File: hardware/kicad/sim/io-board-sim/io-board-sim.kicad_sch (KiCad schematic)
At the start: 74 parts, among them J1 to L IN combo jack, J2 to R IN combo jack, J3 to L OUT combo jack, J4 to R OUT combo jack, P1 JIO-PWR B3P-VH-B, P2 P2, P3 P3, P4 P4, P5 P5, P6 P6, U1 OPA1644AIDR, U2 OPA1656IDR, U3 OPA1656IDR, U4 OPA1656IDR

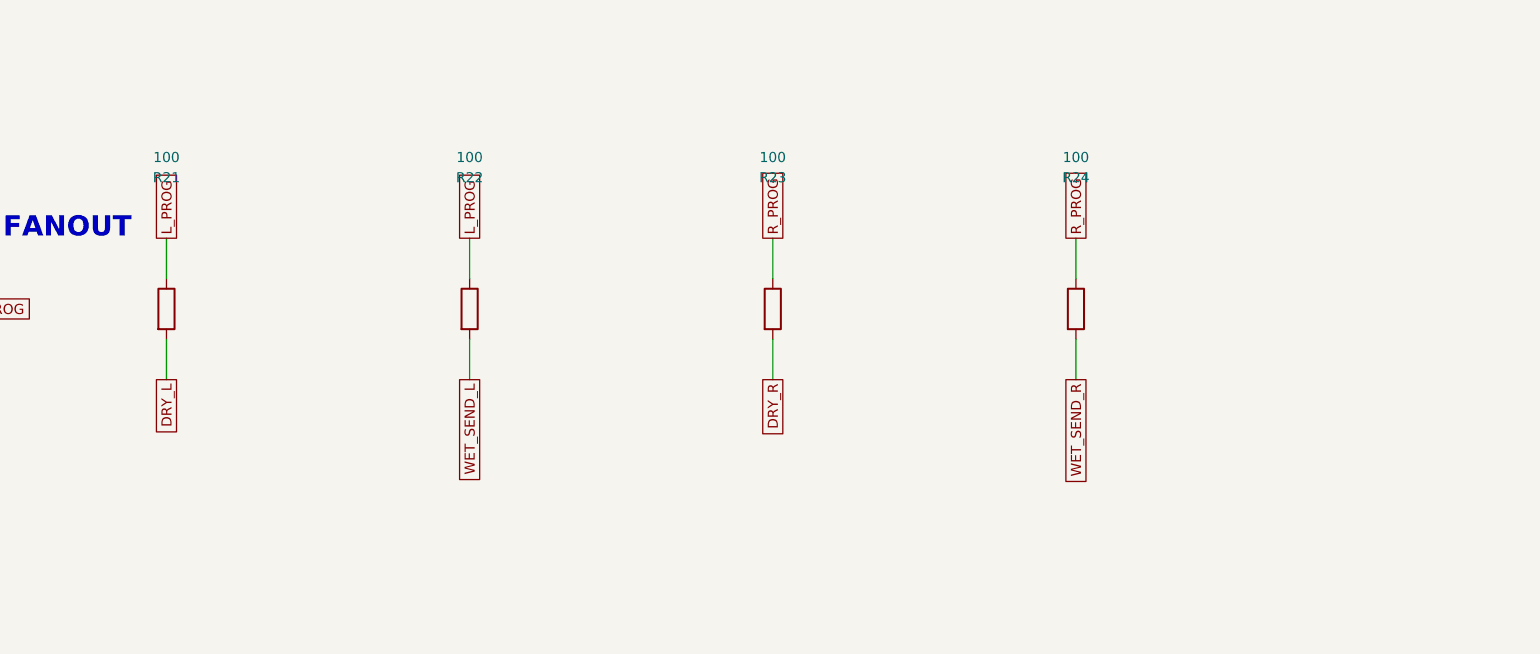
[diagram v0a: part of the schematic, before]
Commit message: Schematic review (kicad-schematic-review skill): F1 R-78E moved to +15VRAW, F2 mono-float bleed R25; both boards re-routed/verified; datasheet cache, per-instance reviews, schematic_review.md
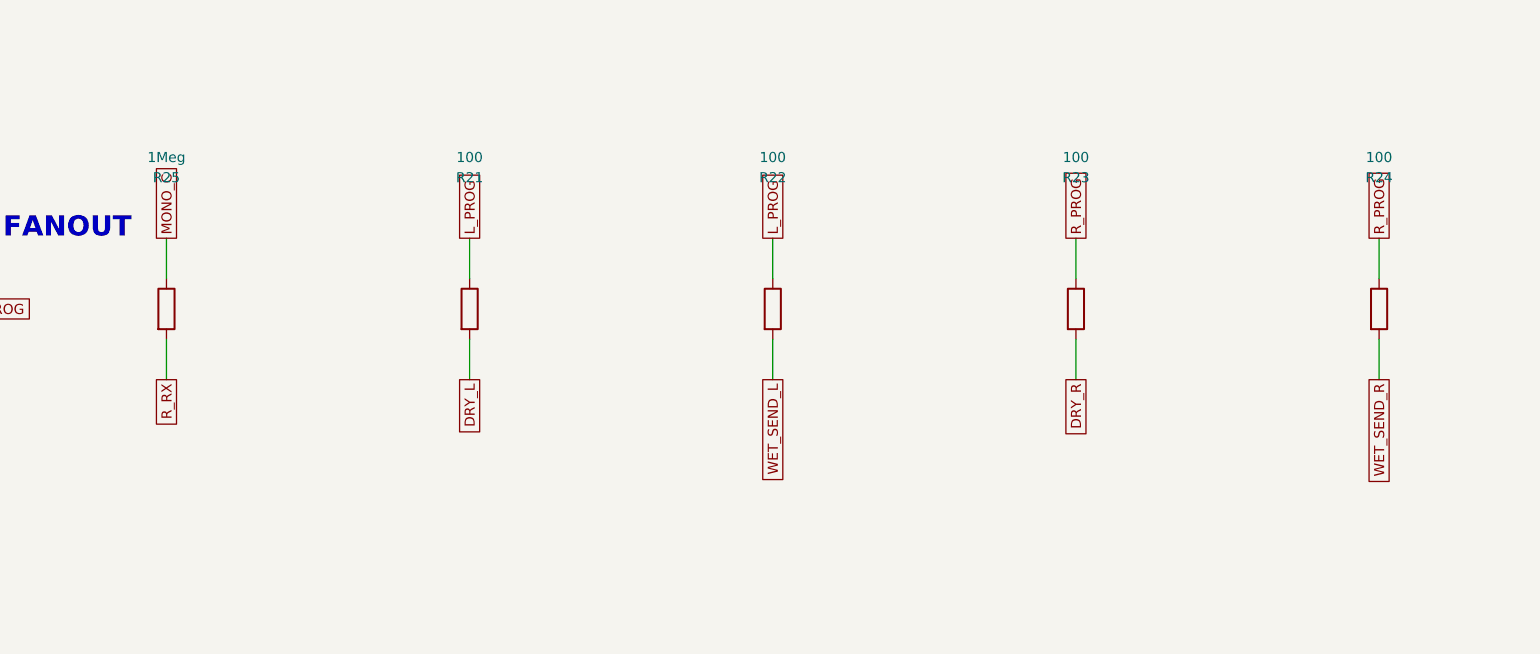
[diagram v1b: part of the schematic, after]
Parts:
- removed R1, R21, R3: 100, Resistor_SMD:R_0805_2012Metric, symbol Device:R
- removed R31: 20k, Resistor_SMD:R_0805_2012Metric, symbol Device:R
- removed R43, R44, R53: 10k, Resistor_SMD:R_0805_2012Metric, symbol Device:R
- removed unit 5 of U1
- removed unit 3 of U2
- removed V1, V2: 15V, symbol Simulation_SPICE:VDC
- added C100, C99: 22u, Capacitor_SMD:C_1210_3225Metric, symbol Device:C
- added R23, R24: 100, Resistor_SMD:R_0805_2012Metric, symbol Device:R
- added R50, R60: 49.9, Resistor_SMD:R_0805_2012Metric, symbol Device:R
- added RL3, RL4: 10k, Resistor_SMD:R_0805_2012Metric, symbol Device:R
- added unit 2 of U1
- added unit 1 of U1
- added unit 2 of U2
- added unit 1 of U4
- C2: renamed from R11; value 10k -> 220p; footprint Resistor_SMD:R_0805_2012Metric -> Capacitor_SMD:C_0805_2012Metric; symbol Device:R -> Device:C; Tolerance 0.1% -> (none); now not fitted
- C4: renamed from R15; value 10k -> 220p; footprint Resistor_SMD:R_0805_2012Metric -> Capacitor_SMD:C_0805_2012Metric; symbol Device:R -> Device:C; Tolerance 0.1% -> (none); now not fitted
- C97: renamed from C99; value 22u -> 100n; footprint Capacitor_SMD:C_1210_3225Metric -> Capacitor_SMD:C_0805_2012Metric
- C98: renamed from C100; value 22u -> 100n; footprint Capacitor_SMD:C_1210_3225Metric -> Capacitor_SMD:C_0805_2012Metric
- R14, R18: renamed from U1; value OPA1644AIDR -> 10k; footprint Package_SO:SOIC-14_3.9x8.7mm_P1.27mm -> Resistor_SMD:R_0805_2012Metric; symbol Amplifier_Operational:TL074 -> Device:R; Tolerance (none) -> 0.1%
- R2: renamed from C1; value 220p -> 100; footprint Capacitor_SMD:C_0805_2012Metric -> Resistor_SMD:R_0805_2012Metric; symbol Device:C -> Device:R; now fitted
- R25: renamed from R22; value 100 -> 1Meg
- R31: renamed from U2; value OPA1656IDR -> 20k; footprint Package_SO:SOIC-8_3.9x4.9mm_P1.27mm -> Resistor_SMD:R_0805_2012Metric; symbol Amplifier_Operational:OPA1656ID -> Device:R
- R4: renamed from C3; value 220p -> 100; footprint Capacitor_SMD:C_0805_2012Metric -> Resistor_SMD:R_0805_2012Metric; symbol Device:C -> Device:R; now fitted
- R43: renamed from R50; value 49.9 -> 10k
- R44: renamed from U4; value OPA1656IDR -> 10k; footprint Package_SO:SOIC-8_3.9x4.9mm_P1.27mm -> Resistor_SMD:R_0805_2012Metric; symbol Amplifier_Operational:OPA1656ID -> Device:R
- R53: renamed from R60; value 49.9 -> 10k
- RL1: renamed from RL3; value 10k -> 600
- RL2: renamed from RL4; value 10k -> 600
- RP3: renamed from RL1; value 600 -> 10k
- RP4: renamed from RL2; value 600 -> 10k
- RS1: renamed from RP2; value 10k -> 0
- U1: renamed from U3; value OPA1656IDR -> OPA1644AIDR; footprint Package_SO:SOIC-8_3.9x4.9mm_P1.27mm -> Package_SO:SOIC-14_3.9x8.7mm_P1.27mm; symbol Amplifier_Operational:OPA1656ID -> Amplifier_Operational:TL074
- U3: renamed from C91; value 100n -> OPA1656IDR; footprint Capacitor_SMD:C_0805_2012Metric -> Package_SO:SOIC-8_3.9x4.9mm_P1.27mm; symbol Device:C -> Amplifier_Operational:OPA1656ID
- U4: renamed from C92; value 100n -> OPA1656IDR; footprint Capacitor_SMD:C_0805_2012Metric -> Package_SO:SOIC-8_3.9x4.9mm_P1.27mm; symbol Device:C -> Amplifier_Operational:OPA1656ID
- V1: renamed from V3; value 0V bond -> 15V
- V2: renamed from V4; value +0.5 1kHz -> 15V; symbol Simulation_SPICE:VSIN -> Simulation_SPICE:VDC
- V3: renamed from V5; value -0.5 1kHz -> 0V bond; symbol Simulation_SPICE:VSIN -> Simulation_SPICE:VDC
- V6: renamed from V8; value 0.3 500Hz -> +0.5 1kHz
- V7: renamed from V9; value 0.3 500Hz -> -0.5 1kHz
- V8: renamed from RS1; value 0 -> 0.3 500Hz; footprint Resistor_SMD:R_0805_2012Metric -> (none); symbol Device:R -> Simulation_SPICE:VSIN
- V9: renamed from RP1; value 10k -> 0.3 500Hz; footprint Resistor_SMD:R_0805_2012Metric -> (none); symbol Device:R -> Simulation_SPICE:VSIN
- renumbered C2 to C1, C4 to C3, C93 to C91, C94 to C92, C95 to C93, C96 to C94, C97 to C95, C98 to C96, R2 to R1, R12 to R11, R13 to R12, R14 to R13, R16 to R15, R17 to R16, R18 to R17, R23 to R21, R24 to R22, R4 to R3, RP3 to RP1, RP4 to RP2, U4 to U2, V6 to V4, V7 to V5
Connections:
- net +15VA: now also U1.4 (V+), U3.8 (V+), U4.8 (V+), V1.1, C99.1; no longer U1.8 (V+), U3.1
- net -15VA: now also U1.11 (V-), U3.4 (V-), U4.4 (V-), V2.2, C100.1; no longer U1.4 (V-), U4.1
- net AGND: now also C2.2, C4.2, R14.2, R18.2, V3.1, V8.2, V9.2, C100.2, C99.2, RL3.2, RL4.2, U2.5 (+); no longer R13.2, R17.2, R2.2, R31.5 (+), R4.2, RL1.2, RL2.2, U3.2, U4.2, V1.1, V2.2, V3.2
- net DRY_L: now also R21.2, RL4.1; no longer RL2.1
- net DRY_R: now also R23.2; no longer R21.2
- net GND: now also V2.1, V3.2
- net IN_BAL_L_N: now also C2.1, R2.1, V5.1; no longer C1.1, R1.1, V3.1
- net IN_BAL_L_P: now also C1.1, R1.1, V4.1; no longer R2.1, V2.1
- net IN_BAL_R_N: now also C4.1, R4.1, V7.1; no longer C3.1, R3.1, V5.1
- net IN_BAL_R_P: now also C3.1, R3.1, V6.1; no longer R4.1, V4.1
- net L_BLEND: now also R43.1
- net L_PROG: now also R21.1, R22.1, RP1.1; no longer R25.1, V9.1
- net L_RX: now also R12.1, U1.1; no longer R11.1, R14.1
- net MONO_C: now also R25.1, RS1.2; no longer V8.2
- net N_COLD_L: now also R44.1, R50.1; no longer R43.1
- net N_COLD_R: now also R60.1; no longer R53.1
- net N_HOT_R: now also U4.1, U4.2 (-); no longer R44.1, R44.2 (-)
- net N_INL_N: now also R11.1, R2.2; no longer C2.1, R1.2
- net N_INL_P: now also R1.2, R13.1; no longer R12.1
- net N_INR_N: now also R15.1, R4.2; no longer C4.1, R3.2
- net N_INR_P: now also R17.1, R3.2; no longer R16.1
- net N_U1A_M: now also R12.2, U1.2 (-); no longer C2.2, R14.2 (-)
- net N_U1A_P: now also R13.2, R14.1, U1.3 (+); no longer R12.2, R13.1, R14.3 (+)
- net N_U1B_M: now also R16.2, U1.6 (-); no longer C4.2, R18.6 (-)
- net N_U1B_P: now also R17.2, R18.1, U1.5 (+); no longer R16.2, R17.1, R18.5 (+)
- net N_U2A_M: now also R31.2
- net N_U2B_M: now also U2.6 (-); no longer R31.6 (-)
- net N_U3B_M: now also R43.2, R44.2
- net N_U4B_M: now also R53.2
- net OUT_BAL_L_N: now also RL1.2, R50.2; no longer R43.2, RP3.2
- net OUT_BAL_L_P: now also RL1.1; no longer RP3.1
- net OUT_BAL_R_N: now also RL2.2, R60.2; no longer R53.2, RP4.2
- net OUT_BAL_R_P: now also RL2.1; no longer RP4.1
- net R_BLEND: now also R53.1, U2.7, U4.3 (+); no longer R31.7, R44.3 (+)
- net R_PROG: now also RP3.1, R23.1, R24.1; no longer R21.1, R22.1, RP1.1
- net R_RX: now also R16.1, R25.2, RS1.1, U1.7; no longer R15.1, R18.7, V8.1
- net WD_L_WIPER: now also R31.1, RP1.2, RP2.1; no longer RS1.1, V9.2
- net WD_R_WIPER: now also RP3.2, RP4.1; no longer RP1.2, RP2.1
- net WET_SEND_L: now also R22.2, RL3.1; no longer R25.2, RL1.1
- net WET_SEND_R: now also R24.2; no longer R22.2
- net WET_SUM_L: now also RP2.2, V8.1; no longer RS1.2, V6.1
- net WET_SUM_R: now also RP4.2, V9.1; no longer RP2.2, V7.1
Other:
- moved on the sheet: C1, C3, C91, C92, C93, C94, C95, C96, C97, C98, R1, R11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
